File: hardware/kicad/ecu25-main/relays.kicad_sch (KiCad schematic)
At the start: 31 parts, among them J8 Screw_Terminal_RELAY_OUT, K1 G5LE-1 24V, K2 G5LE-1 24V, K3 G5LE-1 24V, K4 G5LE-1 24V, K5 G5LE-1 24V, K6 G5LE-1 24V, Q60 2N7002K 60V, Q61 2N7002K 60V, Q62 2N7002K 60V, Q63 2N7002K 60V, Q64 2N7002K 60V, Q65 2N7002K 60V

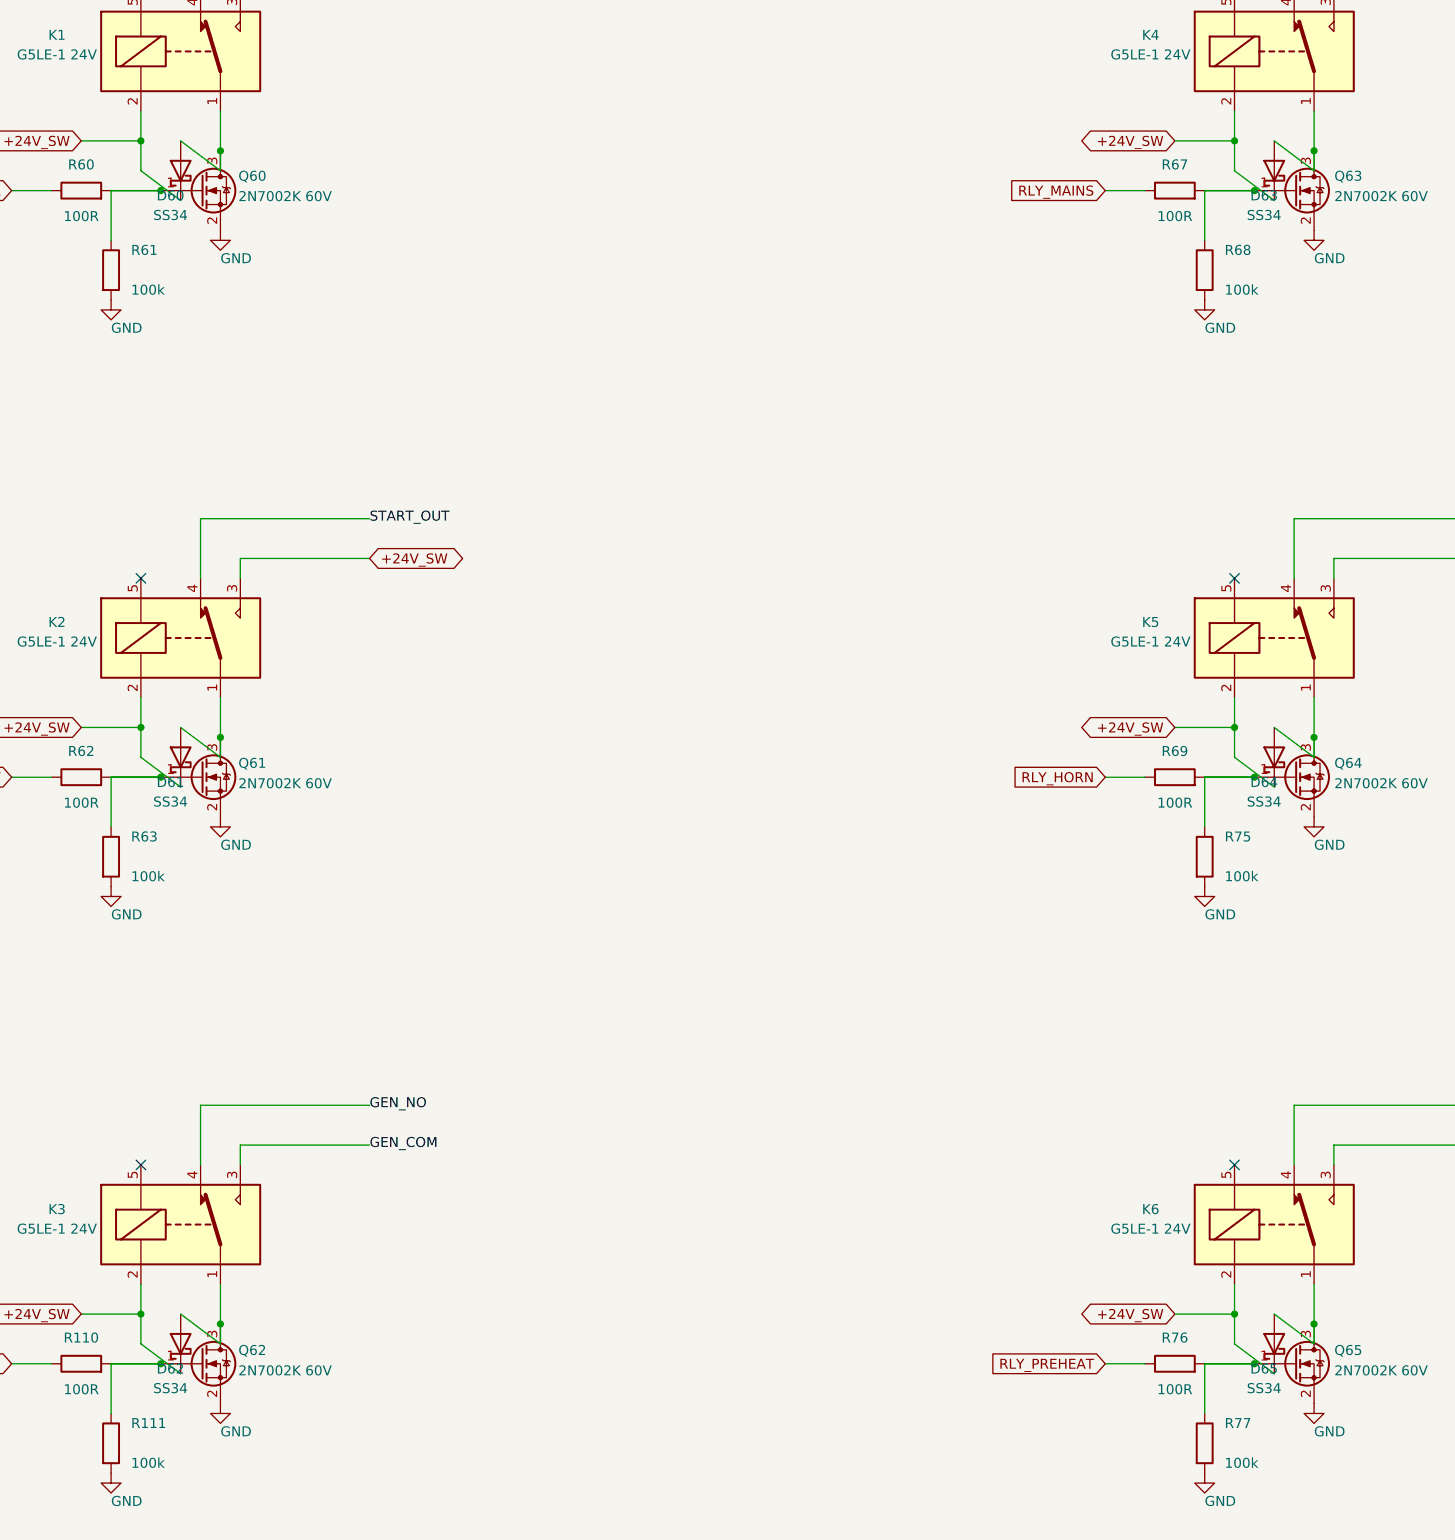
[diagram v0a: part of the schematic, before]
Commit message: Fix SME review findings: 3 critical, 6 major schematic faults
Critical:
- RON pin no longer shorted to GND (R4 moved off C3's column)
- LM2903 MPU comparator +/- inputs unmerged (separate route columns)
- Supercap charge diode D70 un-reversed (anode to +3V3)

Major:
- Buck UVLO divider restored (stray EN stub ended on C3 column = EN
  tied to +24V; stub removed)
- RS485 fail-safe bias polarity corrected (pull-up A, pull-down B)
- U8 spare op-amp unit placed and tied off (was floating on VREF die)
- Heartbeat LED DS1 un-reversed
- VREF_MID buffer dual feedback added (R93 DC path + C93 AC path)
- D80 value SMBJ33A -> SMBJ33CA (bidirectional, matches symbol)

Added netlist-level sweep check (shorted 2-pin devices, rail
membership) since the geometric tracer is blind to shorts closed
through power symbols across wire islands. Sweep: CLEAN, 0 issues.
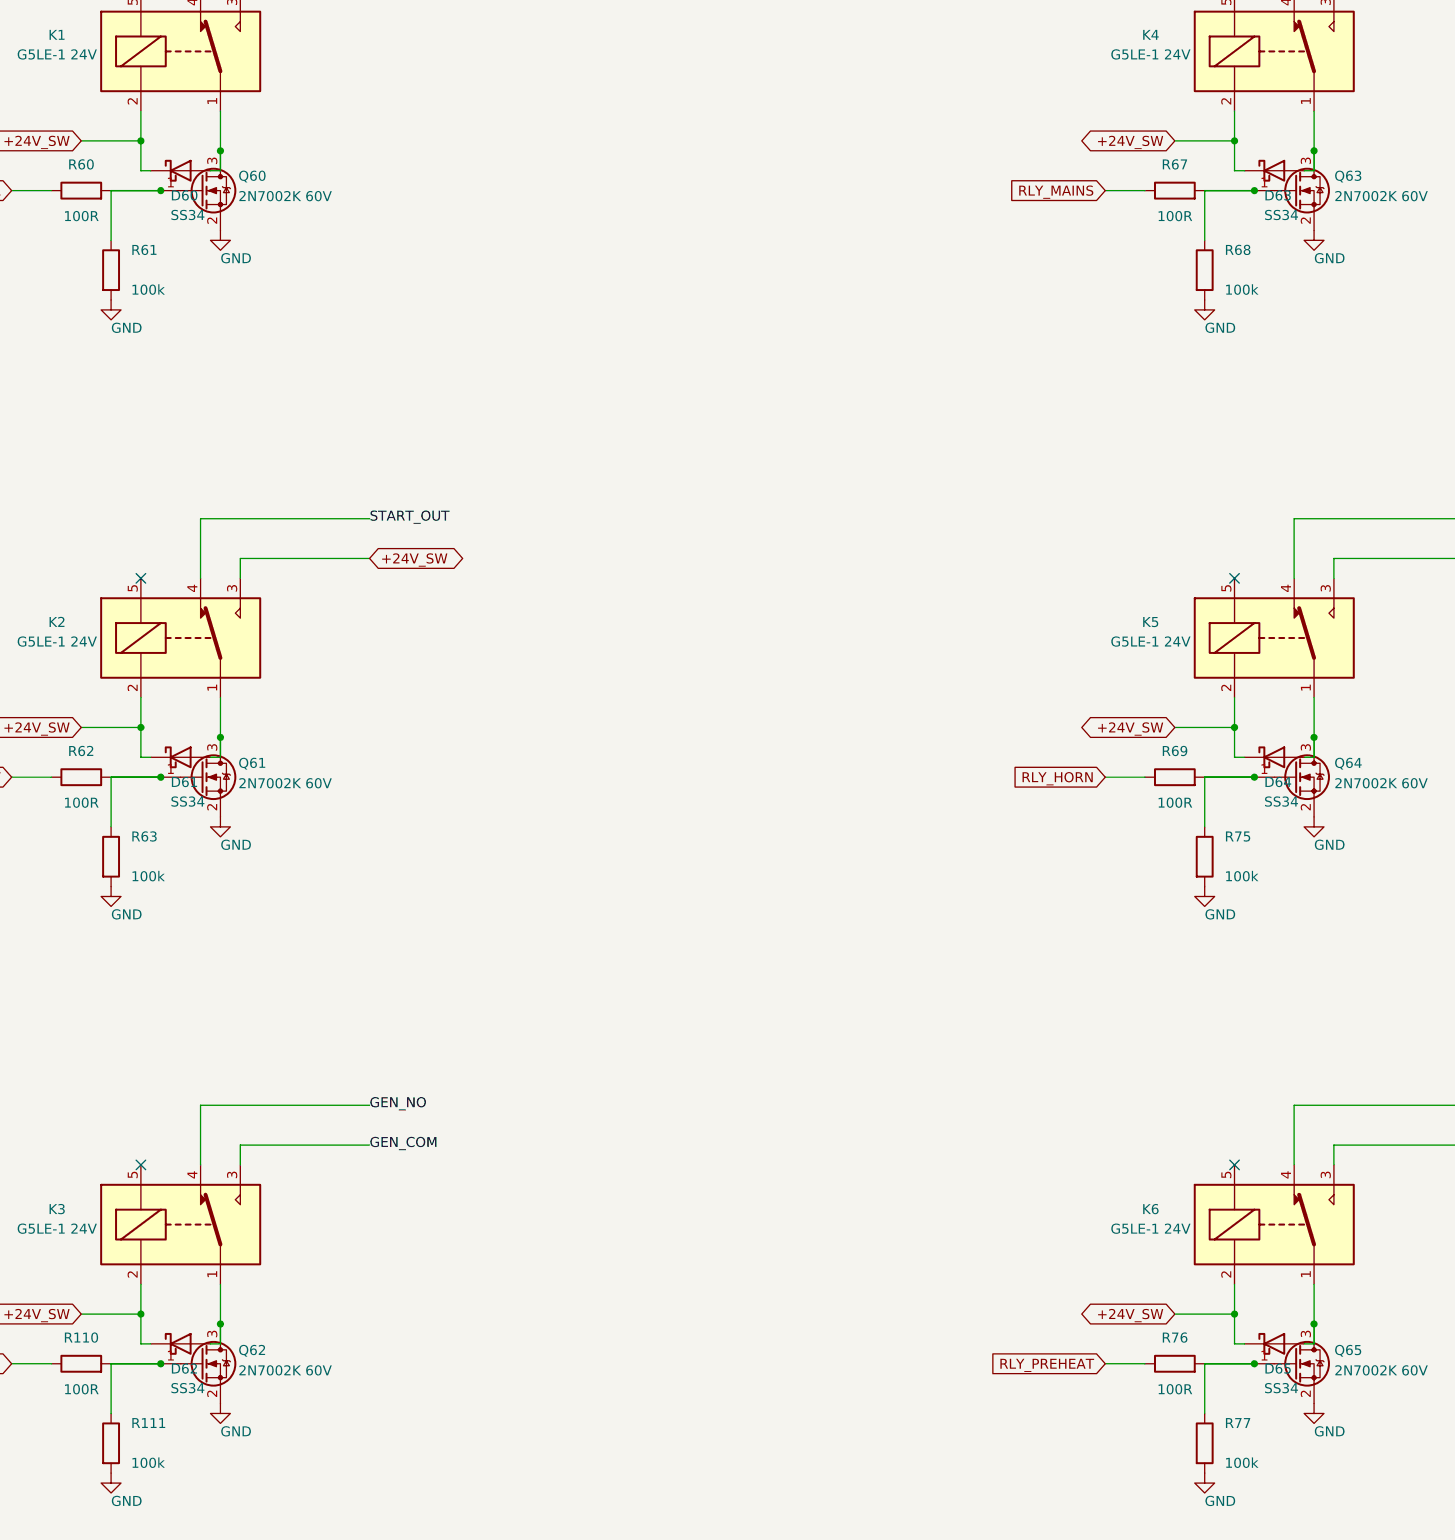
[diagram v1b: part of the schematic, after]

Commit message: Assign footprints to all 299 components in schematic generator
- By-ref exceptions + per-symbol defaults + value rules (wattage/voltage classes)
- Field connectors: MKDS-3 for battery/AC/CT/relay terminals, MKDS-1,5 for signal
- Q1 reverse-protection FET: Q_PMOS_GSD -> Q_PMOS_GDS + TO-252-2 (DPAK pad
  numbering 1=G 2=D 3=S; GSD variant would swap D/S in the netlist), part
  SQD50P06-15L
- Verified: all footprint files exist in KiCad 7 libs, all symbol pin numbers
  present in footprint pads, netlist sweep still clean
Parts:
- D60, D61, D62, D63, D64, D65: footprint (none) -> Diode_SMD:D_SMA
- J8: footprint (none) -> TerminalBlock_Phoenix:TerminalBlock_Phoenix_MKDS-3-8-5.08_1x08_P5.08mm_Horizontal
- K1, K2, K3, K4, K5, K6: footprint (none) -> Relay_THT:Relay_SPDT_Omron-G5LE-1
- Q60, Q61, Q62, Q63, Q64, Q65: footprint (none) -> Package_TO_SOT_SMD:SOT-23
- R110, R111, R60, R61, R62, R63, R67, R68, R69, R75, R76, R77: footprint (none) -> Resistor_SMD:R_0603_1608Metric

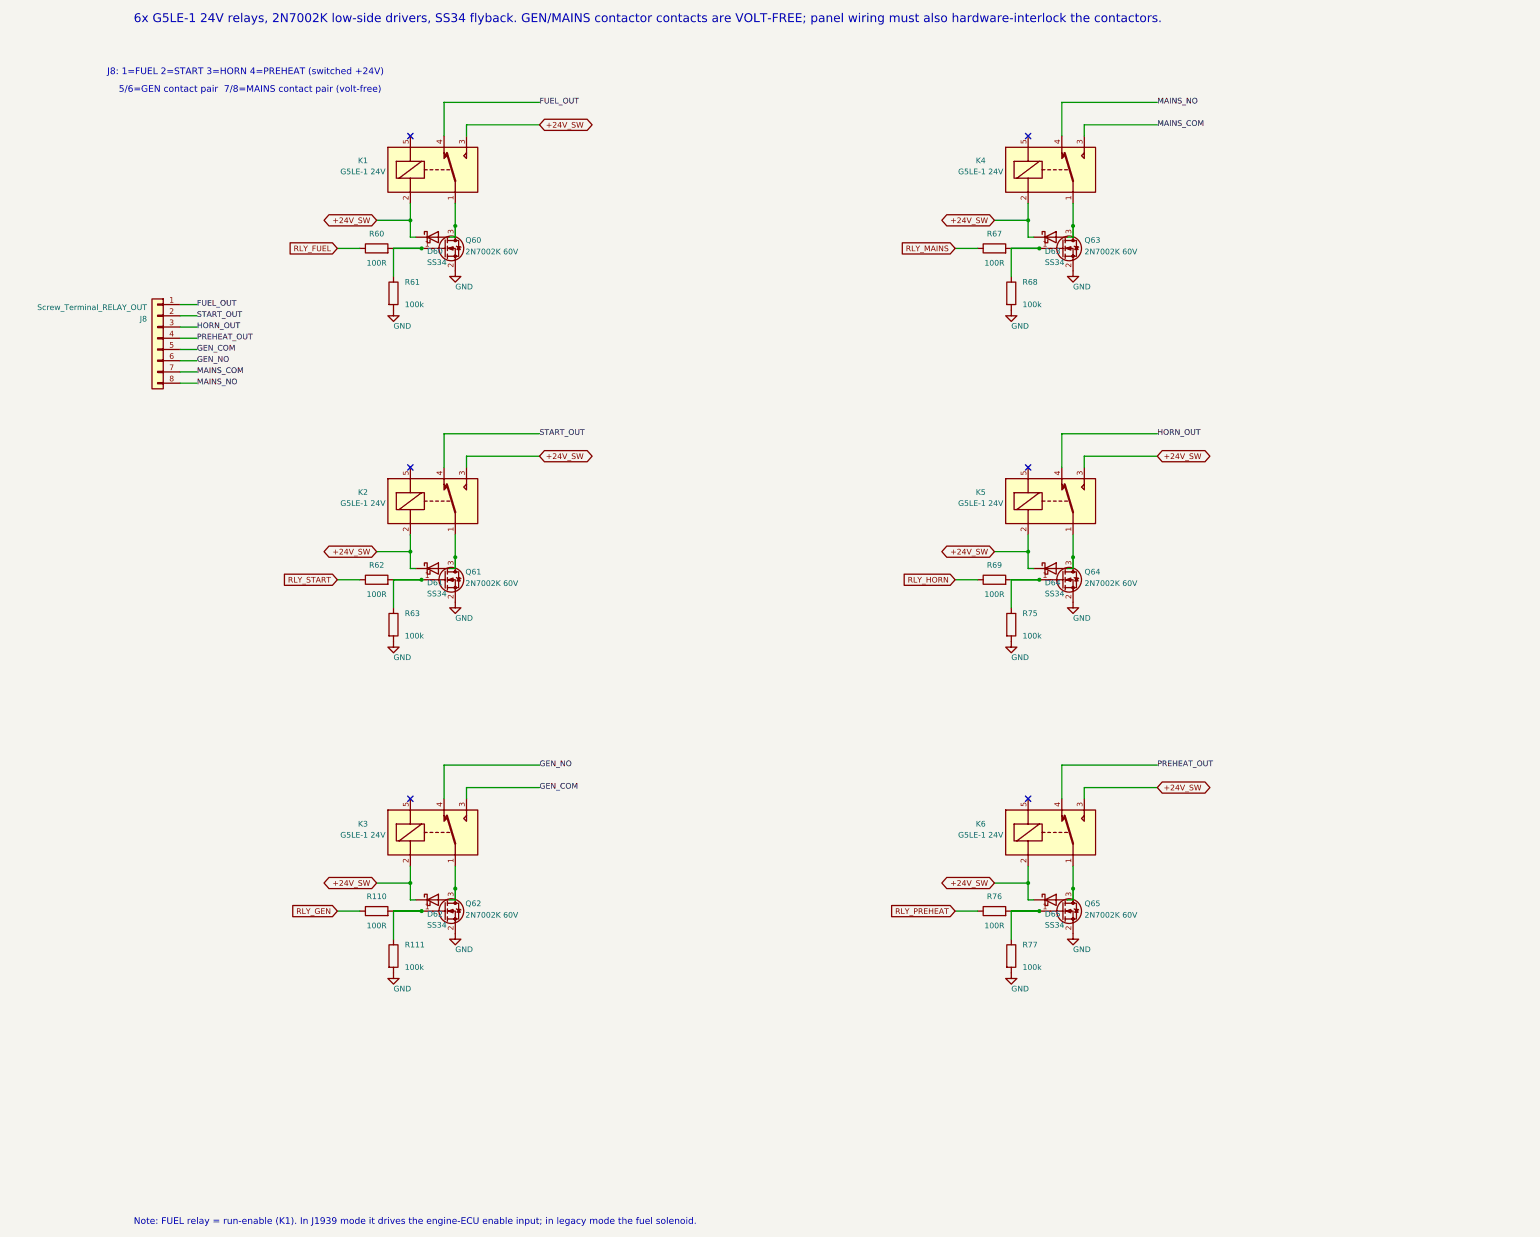
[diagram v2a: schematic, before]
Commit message: Fix PCB SME review findings: relay pin map, 415V clearances, terminal creepage
CRITICAL: G5LE-1 pin map — lib symbol/footprint has coil on pins 2/5, COM 1,
NO 3, NC 4; generator assumed 1/2 coil + 3/4/5 contacts, netting all six
relays dead (coil open, outputs on NC, volt-free GEN/MAINS contacts tied to
logic GND through the driver FETs). Relay sheet rewired, verified by netlist.

MAJOR fixes, all generator-side:
- Volt-free contactor pairs split off J8 onto new J15; J5/J6/J15 are 8-pole
  5.08mm blocks with only odd poles wired (10.16mm live pitch) + pad remap —
  fully-populated 400V-class blocks don't meet PD2 creepage for 415V L-L /
  unsynchronized-source spacing
- DRU rebuilt: GND no longer swept into the line class (was making the board
  unroutable), 3.0mm line class now includes the J15 contactor nets, per-chain
  1.0mm exemptions so the first 330k doesn't false-trip, netless-pad rule,
  generated-file header
- Copper-pour keepouts under J5/J6, the 330k chains, and the volt-free
  contact corridor K3/K4 -> J15
- CT burden + TVS fixed at J7; buck hot loop (C3/U1/L2/C5/C6) and input chain
  fixed in electrical order; R88 (2.6W) moved to the board edge away from
  precision analog; packer margin 0.4 -> 0.6mm
- F2 PTC now specified 60V (sees the 53V load-dump clamp while tripped)

Docs + diagrams + PDFs synced; verified: no overlaps, nothing outside
outline, odd-pole remap correct on J5/J6/J15, netlist sweep clean
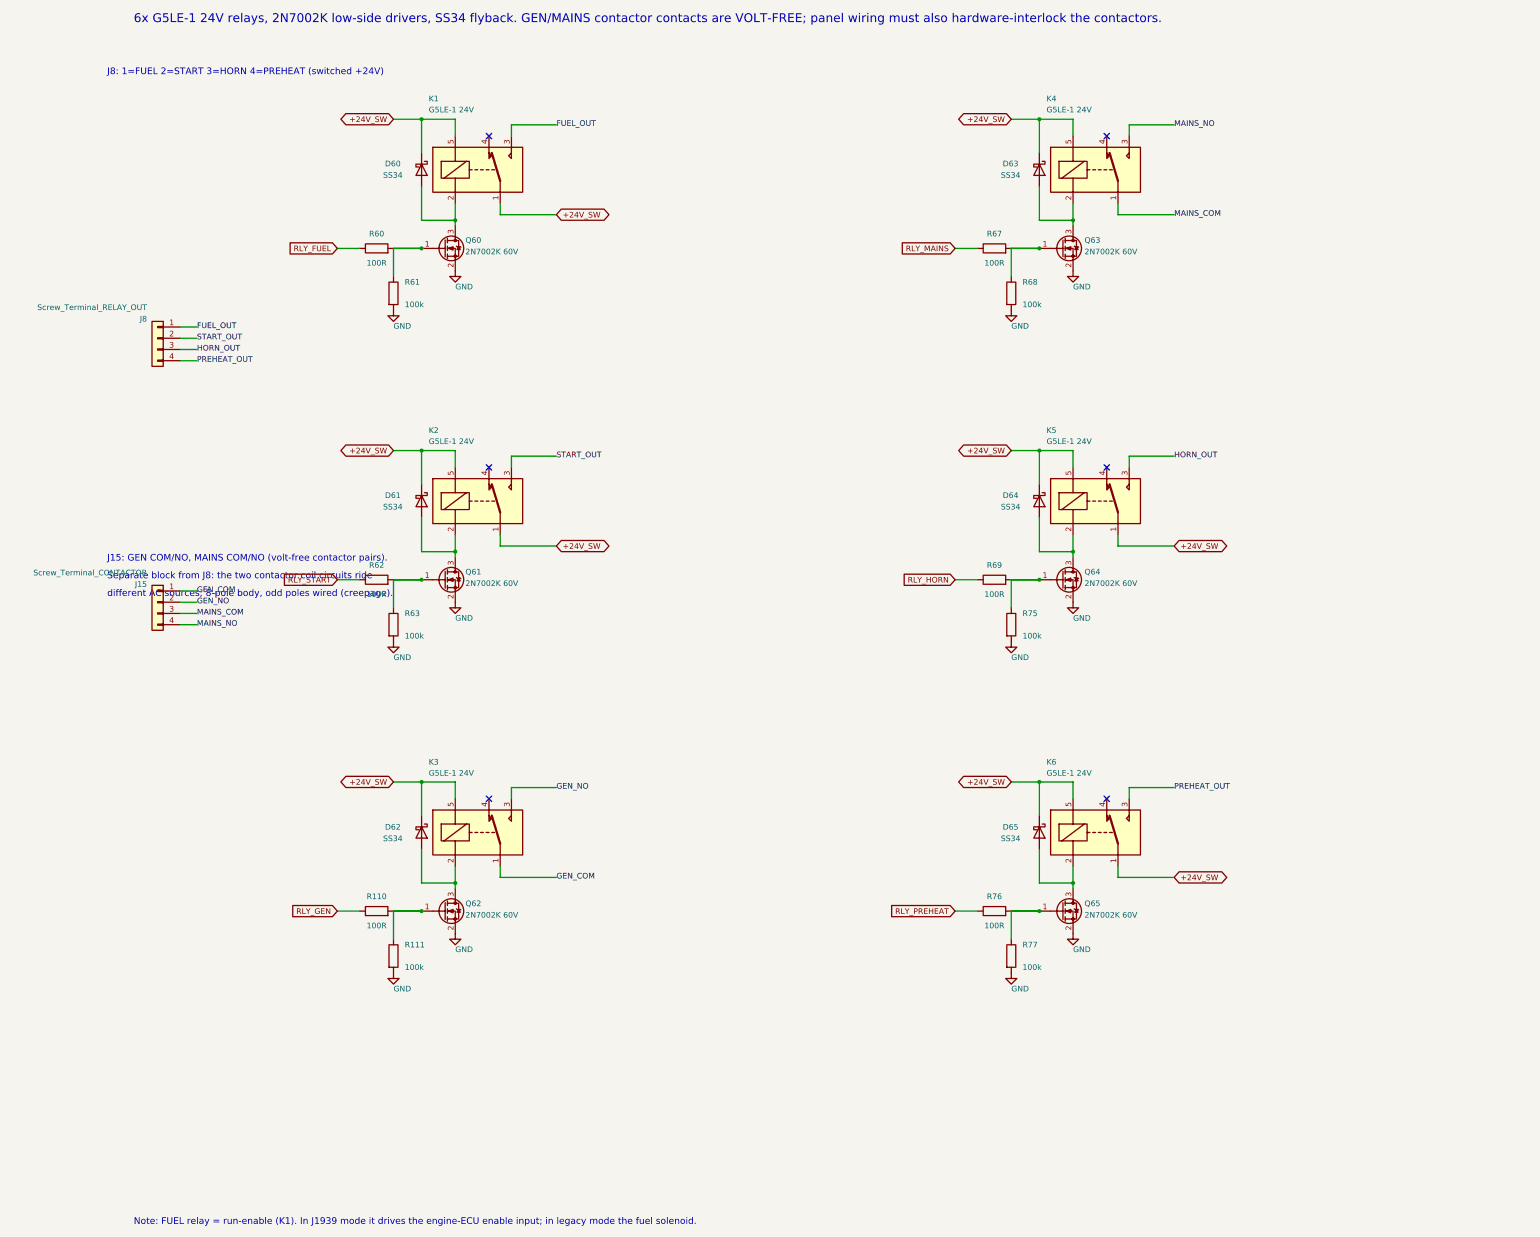
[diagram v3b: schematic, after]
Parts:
- removed J8: Screw_Terminal_RELAY_OUT, TerminalBlock_Phoenix:TerminalBlock_Phoenix_MKDS-3-8-5.08_1x08_P5.08mm_Horizontal, symbol Connector_Generic:Conn_01x08
- added J15: Screw_Terminal_CONTACTOR, TerminalBlock_Phoenix:TerminalBlock_Phoenix_MKDS-3-8-5.08_1x08_P5.08mm_Horizontal, symbol Connector_Generic:Conn_01x04
- added J8: Screw_Terminal_RELAY_OUT, TerminalBlock_Phoenix:TerminalBlock_Phoenix_MKDS-3-4-5.08_1x04_P5.08mm_Horizontal, symbol Connector_Generic:Conn_01x04
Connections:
- net +24V_SW: now also K1.1, K1.5, K2.1, K2.5, K3.5, K4.5, K5.1, K5.5, K6.1, K6.5; no longer K1.2, K1.3, K2.2, K2.3, K3.2, K4.2, K5.2, K5.3, K6.2, K6.3
- net FUEL_OUT: now also K1.3, J8.1 (Pin_1); no longer K1.4
- net GEN_COM: now also K3.1, J15.1 (Pin_1); no longer K3.3
- net GEN_NO: now also K3.3, J15.2 (Pin_2); no longer K3.4
- net HORN_OUT: now also K5.3, J8.3 (Pin_3); no longer K5.4
- net MAINS_COM: now also K4.1, J15.3 (Pin_3); no longer K4.3
- net MAINS_NO: now also K4.3, J15.4 (Pin_4); no longer K4.4
- net PREHEAT_OUT: now also K6.3, J8.4 (Pin_4); no longer K6.4
- net START_OUT: now also K2.3, J8.2 (Pin_2); no longer K2.4
- net at D62.2 (A), Q62.3 (D): now also K3.2; no longer K3.1
- net at D63.2 (A), Q63.3 (D): now also K4.2; no longer K4.1
- net at D60.2 (A), Q60.3 (D): now also K1.2; no longer K1.1
- net at D61.2 (A), Q61.3 (D): now also K2.2; no longer K2.1
- net at D64.2 (A), Q64.3 (D): now also K5.2; no longer K5.1
- net at D65.2 (A), Q65.3 (D): now also K6.2; no longer K6.1
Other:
- note added: "J15: GEN COM/NO, MAINS COM/NO (volt-free contactor pairs)."
- note added: "Separate block from J8: the two contactor coil circuits ride"
- note added: "different AC sources; 8-pole body, odd poles wired (creepage)."
- note removed: "5/6=GEN contact pair 7/8=MAINS contact pair (volt-free)"
